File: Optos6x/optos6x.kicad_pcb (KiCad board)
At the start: 2 copper layers, 32 x 86 mm, 23 parts, among them P1 CONN_01X08, U1 CNY70, U2 CNY70, U3 CNY70, U4 CNY70, U5 CNY70, U6 CNY70

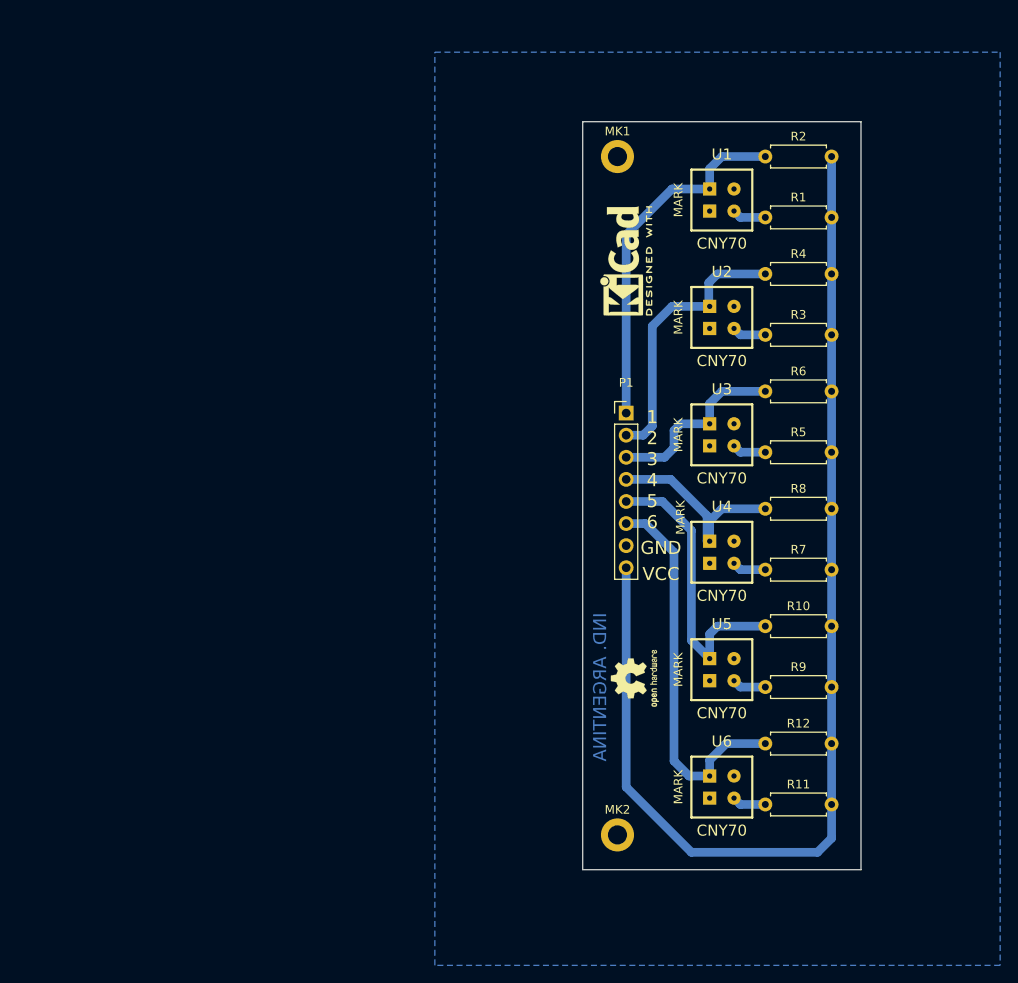
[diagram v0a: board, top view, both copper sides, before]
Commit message: Agrego nombre a la serigrafía y detalles.
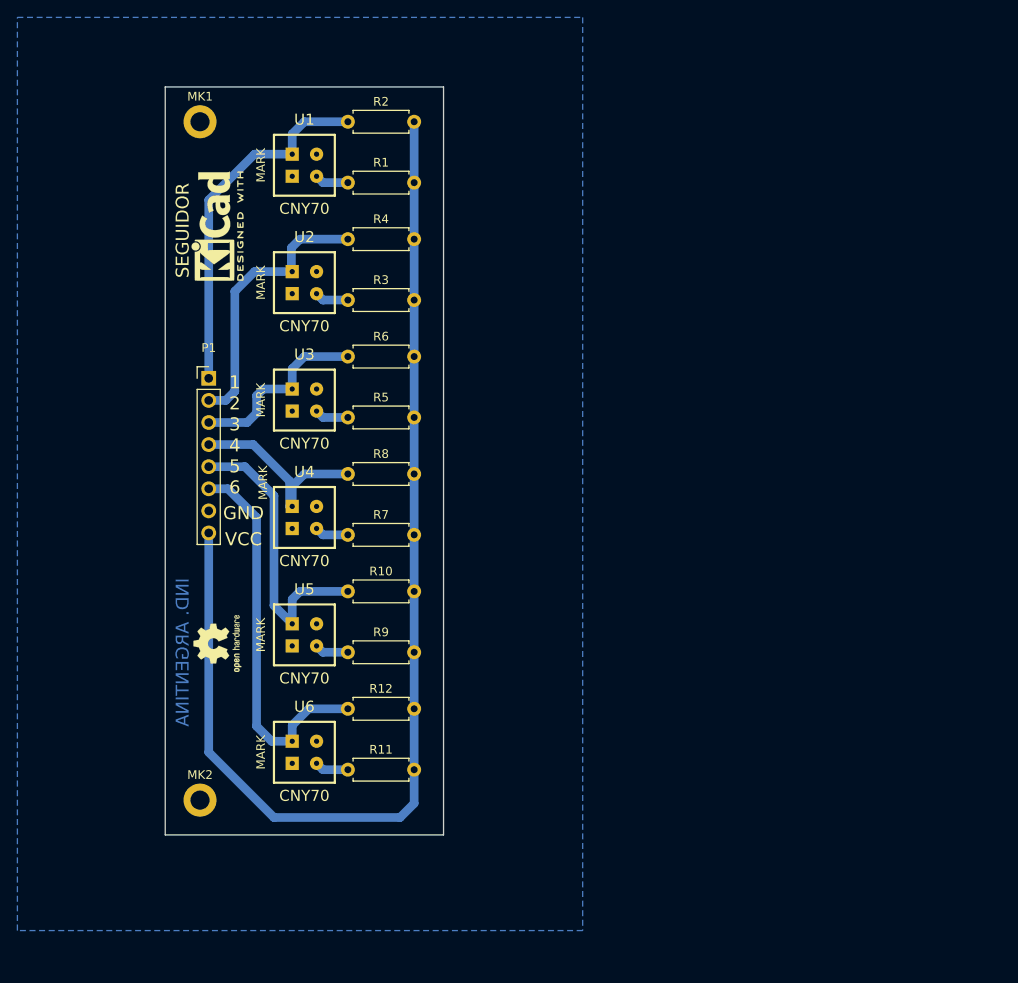
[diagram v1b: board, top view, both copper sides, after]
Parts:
- moved LOGO1 48.2 mm to (124.0, 124.0)
- moved MK1 48.2 mm to (122.0, 64.0)
- moved MK2 48.2 mm to (122.0, 142.0)
- moved P1 48.2 mm to (123.0, 93.5)
- moved R1 48.2 mm to (139.0, 71.0)
- moved R10 48.2 mm to (139.0, 118.0)
- moved R11 48.2 mm to (139.0, 138.5)
- moved R12 48.2 mm to (139.0, 131.5)
- moved R2 48.2 mm to (139.0, 64.0)
- moved R3 48.2 mm to (139.0, 84.5)
- moved R4 48.2 mm to (139.0, 77.5)
- moved R5 48.2 mm to (139.0, 98.0)
- moved R6 48.2 mm to (139.0, 91.0)
- moved R7 48.2 mm to (139.0, 111.5)
- moved R8 48.2 mm to (139.0, 104.5)
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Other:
- board text added: "SEGUIDOR"
